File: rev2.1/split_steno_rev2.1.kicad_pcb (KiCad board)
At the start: 2 copper layers, 99.7 x 74.8 mm, 72 parts, among them J2 Audio-Jack-4, J3 Conn_01x03, P1 TC2030-IDC, SW1 SW_Push, SW10 SW_Push, SW11 SW_Push, SW12 SW_Push, SW13 SW_Push, SW14 SW_Push, SW15 SW_Push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

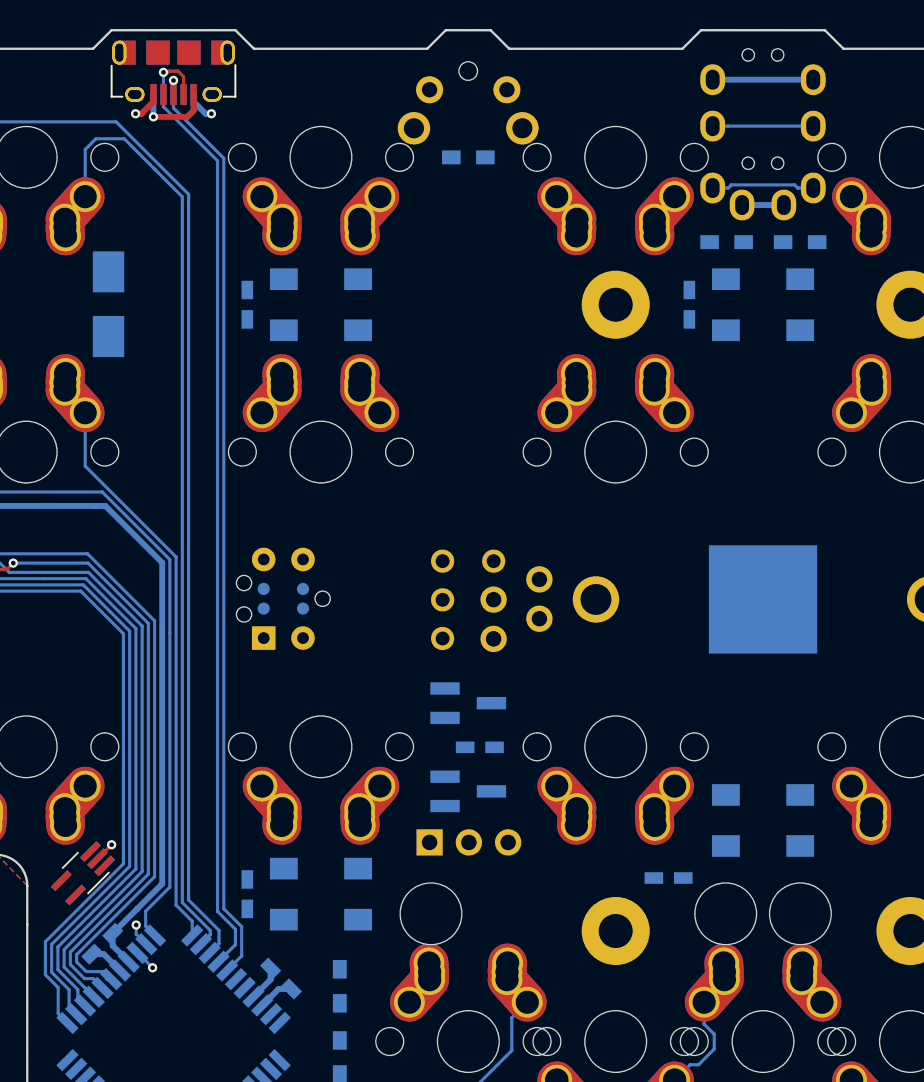
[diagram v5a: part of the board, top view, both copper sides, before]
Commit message: matched differential pair lengths
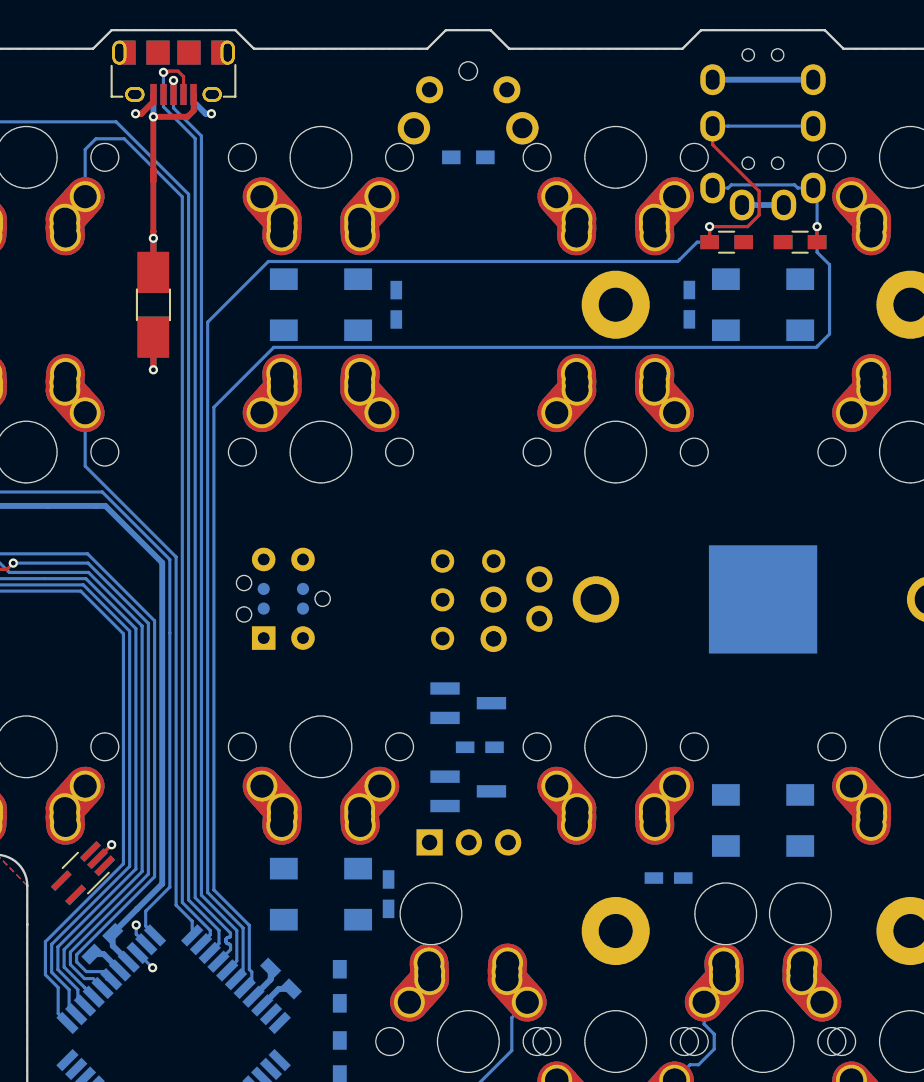
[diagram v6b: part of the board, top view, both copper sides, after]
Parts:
- added REF**: Fuse_SMD1206_HandSoldering, Fuse_Holders_and_Fuses:Fuse_SMD1206_HandSoldering, F.Cu at (67.8, 83.3)
- added REF**: R_0603_HandSoldering, Resistors_SMD:R_0603_HandSoldering, F.Cu at (104.8, 79.3)
- added REF**: R_0603_HandSoldering, Resistors_SMD:R_0603_HandSoldering, F.Cu at (109.5, 79.3)
- moved C3 9.63 mm to (83.5, 83.3)
- moved C6 9.13 mm to (83.0, 121.4)
- moved F1 2.90 mm to (67.8, 83.3)
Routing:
- net /SCL: track 6.67 -> 98.0 mm, vias 0 -> 1
- net /SDA: track 6.50 -> 97.2 mm, vias 0 -> 1
- net Net-(F1-Pad1): track 5.27 -> 18.6 mm, vias 1 -> 2
- net +5V: track 0.00 -> 4.23 mm, vias 0 -> 1

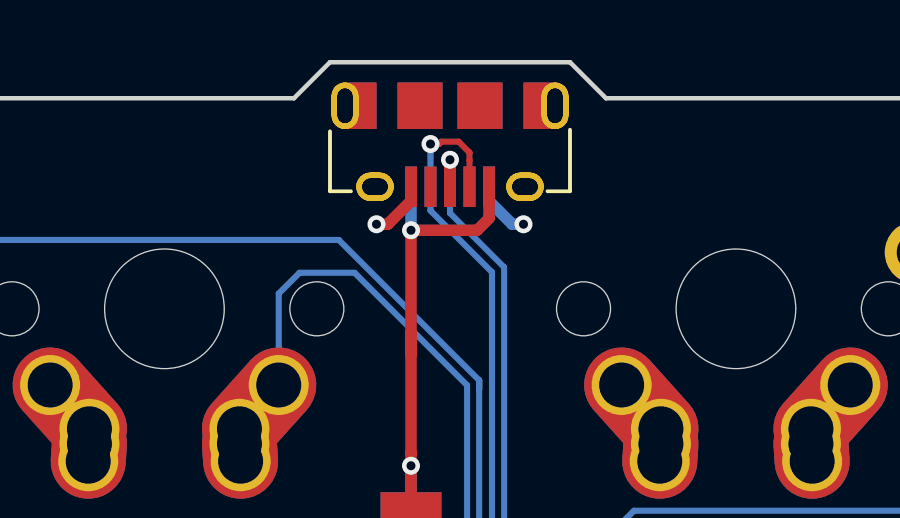
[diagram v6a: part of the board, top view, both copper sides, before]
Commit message: switched from micro to mini b
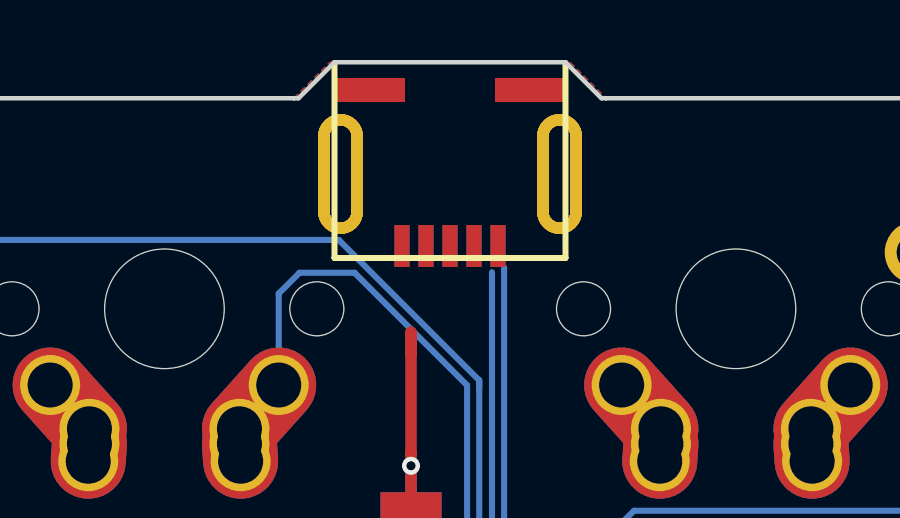
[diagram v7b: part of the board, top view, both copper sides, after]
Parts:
- removed the REF** at (69.0, 67.0)
- removed USB: J1, conn_usb:USB_MicroB_Amphenol_10118194-0001LF
- added J1: USB_OTG, keyboard_parts:USB_miniB_hirose_5S8, B.Cu at (69.0, 71.7)
- added J1: USB_mini_micro_B, keyboard_parts:USB_miniB_hirose_5S8, F.Cu at (69.0, 71.7)
- renumbered RST to SW21, PWR to SW22
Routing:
- net Net-(F1-Pad1): track 18.6 -> 5.12 mm, vias 2 -> 1
- net /D+: track 60.4 -> 55.1 mm, vias 1 -> 0
- net GND: track 48.9 -> 45.0 mm, vias 5 -> 3
- net /D-: track 62.6 -> 59.6 mm, vias 1 -> 0
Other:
- outline, holes or cut-outs redrawn

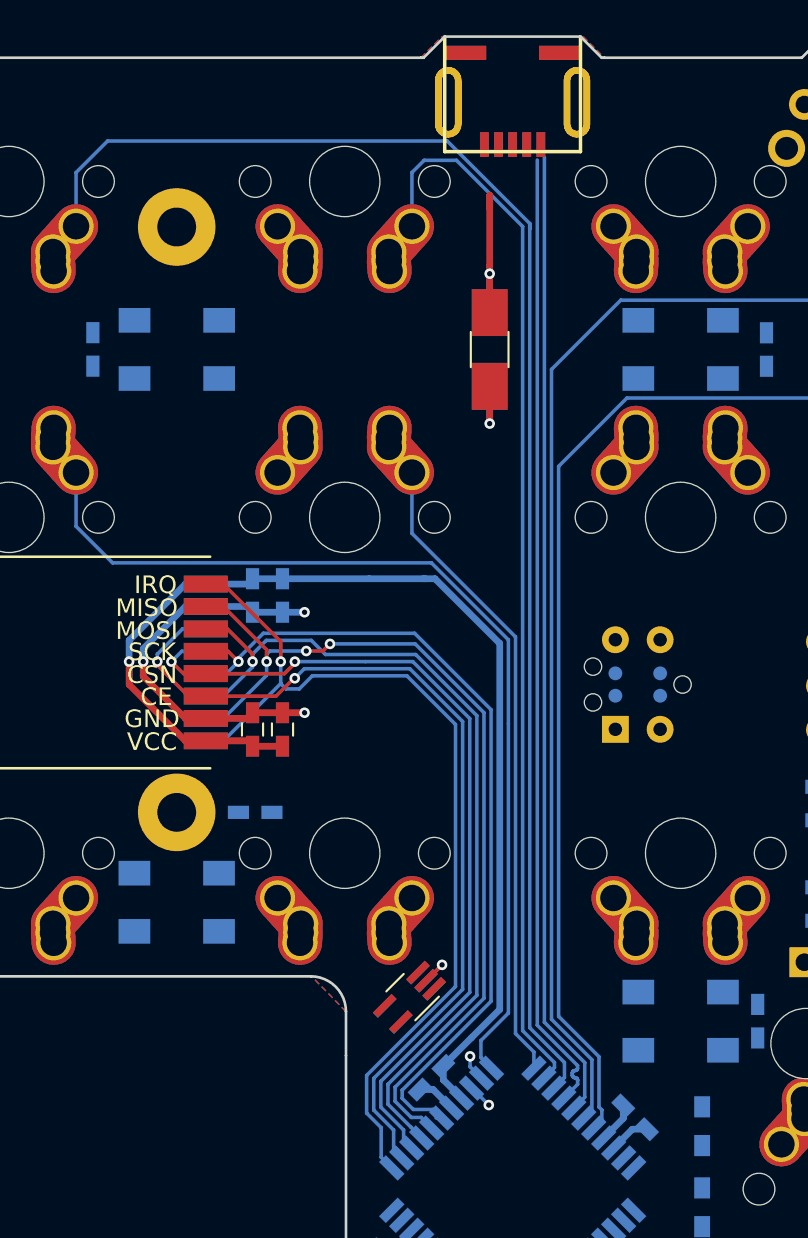
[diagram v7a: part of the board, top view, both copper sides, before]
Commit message: added mini usb and tag connect to both sides
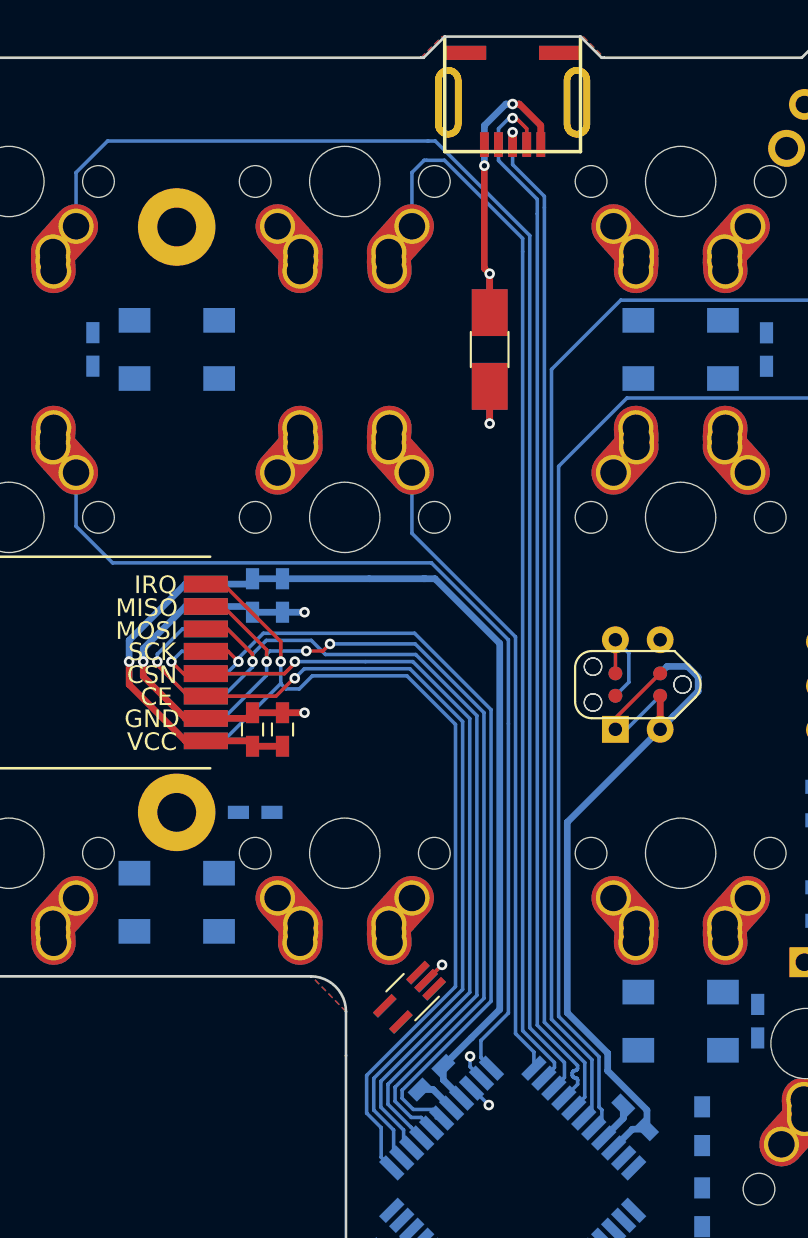
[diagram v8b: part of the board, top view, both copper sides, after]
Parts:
- added TC2030-NL: VAL, Tag-Connect:TC2030-NL_SMALL, F.Cu at (76.2, 102.4)
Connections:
- J1 pad 1: (no net) -> Net-(F1-Pad1)
- J1 pad 2: (no net) -> /D-
- J1 pad 3: (no net) -> /D+
- J1 pad 4: (no net) -> Net-(J1-Pad4)
- J1 pad 5: (no net) -> GND
- J1 pad 6: (no net) -> Net-(J1-Pad6)
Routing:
- net VCC: track 72.3 -> 107.4 mm
- net Net-(F1-Pad1): track 5.12 -> 18.5 mm, vias 1 -> 3
- net /PDI: track 0.00 -> 7.55 mm
- net /RST: track 0.00 -> 5.72 mm
- net /D+: track 55.1 -> 58.0 mm, vias 0 -> 1
- net /D-: track 59.6 -> 60.5 mm, vias 0 -> 1
- net /KEY1: track 81.9 -> 81.2 mm
- net /KEY2: track 60.6 -> 60.1 mm
